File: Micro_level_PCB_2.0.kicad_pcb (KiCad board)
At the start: 2 copper layers, 203.2 x 44.5 mm, 105 parts, among them J5 Conn_01x06, J6 Conn_01x07_Female, Q1 SI2304DDS, Q2 SI2304DDS, Q3 SI2304DDS, Q4 SI2304DDS, Q5 SI2304DDS, SW1 FSM2JSMAA, SW2 FSM2JSMAA, SW3 FSM2JSMAA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

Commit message: 4 button up/down
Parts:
- added SW6: FSM2JSMAA, MY_KICAD_LIB:SW_Push_1P1T_NO_6x6mm_H5.0mm, F.Cu at (15.9, 38.1)
- added SW7: FSM2JSMAA, MY_KICAD_LIB:SW_Push_1P1T_NO_6x6mm_H5.0mm, F.Cu at (15.9, 6.35)
- D1: value SMF18A -> 1PGSMA4740HR3G
- moved J6 19.4 mm to (4.08, 23.6), turned to -90 degrees
- moved C16 17.9 mm to (25.8, 20.8)
- moved L1 15.0 mm to (28.1, 20.9), turned to 90 degrees
- moved SW4 6.35 mm to (31.8, 38.1), turned to 90 degrees
- moved SW5 6.35 mm to (31.8, 6.35), turned to 90 degrees
- renumbered Dimmer to Dim1, Power to Power1, Sensors to Sensors1, Solenoids to Solenoids1
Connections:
- net DOWN renamed Right_DOWN
- net UP renamed Right_UP
- J6 pad 7: OUTSIDE_VALID -> unconnected-(J6-Pad7)
- U1 pad 1: REMOTE_TRAVEL -> Left_UP
- U1 pad 11: POWERUP -> unconnected-(U1-Pad11)
- U1 pad 2: REMOTE_DOWN -> unconnected-(U1-Pad2)
- U1 pad 25: SPARE1 -> unconnected-(U1-Pad25)
- U1 pad 3: REMOTE_UP -> unconnected-(U1-Pad3)
- U1 pad 43: REMOTE_CAMP -> REMOTE_RU
- U1 pad 44: REMOTE_RU -> Left_DOWN
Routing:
- net Left_UP: track 0.00 -> 54.6 mm, vias 0 -> 2
- net Left_DOWN: track 0.00 -> 33.7 mm
- net Net-(C16-Pad2): track 6.57 -> 24.1 mm
- net REMOTE_LD: track 28.2 -> 41.4 mm, vias 1 -> 0
- net REMOTE_LU: track 26.0 -> 38.6 mm, vias 1 -> 0
- net REMOTE_RD: track 26.9 -> 35.7 mm, vias 1 -> 0
- net Right_DOWN: track 37.5 -> 30.4 mm
- net V5: track 233.7 -> 227.5 mm
- net RX: track 39.1 -> 42.9 mm
- net Right_UP: track 29.9 -> 32.5 mm, vias 2 -> 4
- net REMOTE_RU: track 28.9 -> 29.8 mm, vias 1 -> 0

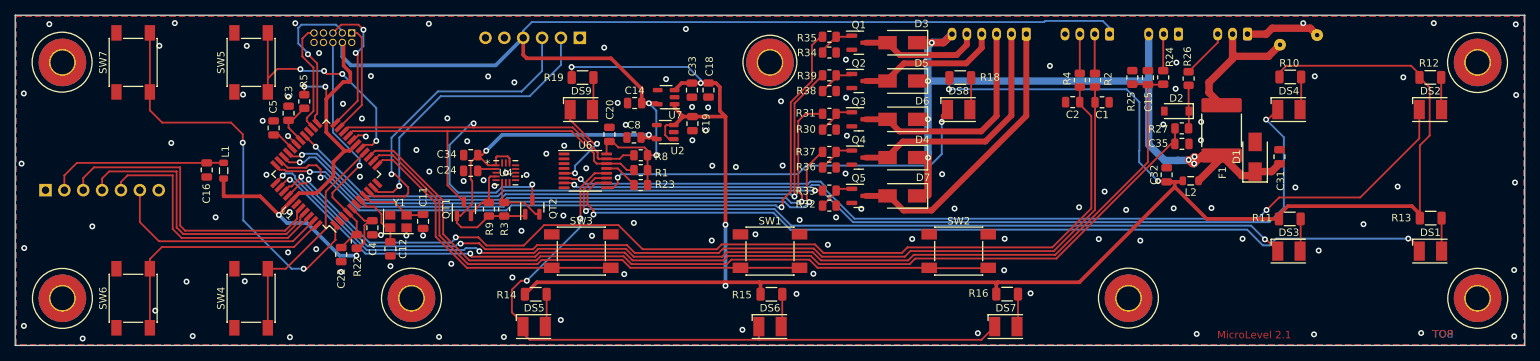
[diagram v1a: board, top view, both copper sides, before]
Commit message: move buttons, change jtag connector
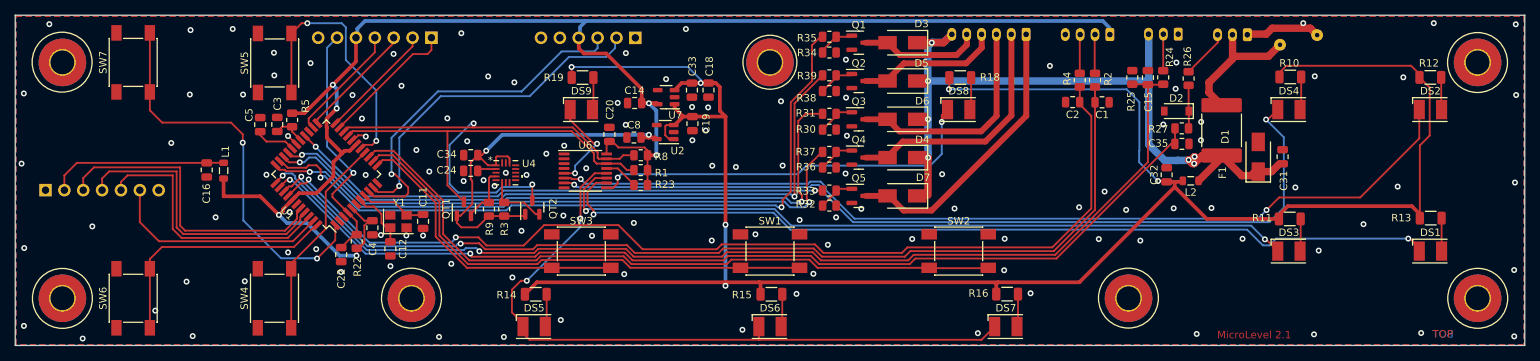
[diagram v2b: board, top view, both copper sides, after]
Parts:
- removed CX1: Conn2x5_CNC#3220-10-0100-00, Connector_PinSocket_1.27mm:PinSocket_2x05_P1.27mm_Vertical
- removed Dim1, Power1: B3B-PH-K-S, Connector_JST:JST_PH_B3B-PH-K_1x03_P2.00mm_Vertical
- removed Sensors1: B4B-PH-K-S, Connector_JST:JST_PH_B4B-PH-K_1x04_P2.00mm_Vertical
- removed Solenoids1: B6B-PH-K-S, Connector_JST:JST_PH_B6B-PH-K_1x06_P2.00mm_Vertical
- added J1: Conn_01x07_Female, Connector_PinHeader_2.54mm:PinHeader_1x07_P2.54mm_Vertical, B.Cu at (56.0, 3.02)
- added J2: B6B-PH-K-S, Connector_JST:JST_PH_B6B-PH-K_1x06_P2.00mm_Vertical, B.Cu at (136.1, 2.58)
- added J3: B3B-PH-K-S, Connector_JST:JST_PH_B3B-PH-K_1x03_P2.00mm_Vertical, B.Cu at (156.6, 2.55)
- added J4: B3B-PH-K-S, Connector_JST:JST_PH_B3B-PH-K_1x03_P2.00mm_Vertical, B.Cu at (165.8, 2.62)
- added j7: B4B-PH-K-S, Connector_JST:JST_PH_B4B-PH-K_1x04_P2.00mm_Vertical, B.Cu at (147.3, 2.60)
- moved J5 7.47 mm to (83.5, 3.04)
- moved SW5 3.18 mm to (34.9, 6.42)
- moved SW4 3.15 mm to (34.9, 38.1)
- moved R5 2.98 mm to (37.3, 14.1)
- moved C3 2.14 mm to (35.3, 14.7)
- moved C5 1.86 mm to (33.0, 14.7)
- moved D1 0.42 mm to (167.3, 19.1)
- moved C31 0.42 mm to (170.6, 19.1)
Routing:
- net V5: track 227.5 -> 216.4 mm
- net TDO: track 20.9 -> 15.1 mm, vias 1 -> 0
- net TX: track 40.1 -> 45.9 mm
- net RX: track 42.9 -> 48.6 mm
- net TMS: track 19.3 -> 15.9 mm, vias 2 -> 0
- net Right_DOWN: track 30.4 -> 26.9 mm
- net TCK: track 15.0 -> 18.4 mm
- net Right_UP: track 32.5 -> 35.9 mm, vias 4 -> 2
- net VLED: track 285.8 -> 283.2 mm
- net Net-(C5-Pad1): track 3.26 -> 5.52 mm
- net Net-(C3-Pad2): track 6.13 -> 4.53 mm
- net LED_ACTIVE: track 95.2 -> 93.9 mm
- net Left_UP: track 54.6 -> 53.4 mm
- net TDI: track 15.2 -> 16.0 mm
- net Net-(C12-Pad1): track 8.25 -> 7.54 mm
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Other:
- board text added: "Compress"
- board text added: "Sensors"
- board text added: "Solenoids"
- board text removed: "Compressor"

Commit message: move resistor
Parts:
- moved R5 0.55 mm to (37.3, 13.6)
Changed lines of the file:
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@@
   )
   (footprint "Resistor_SMD:R_0805_2012Metric" (layer "F.Cu")
-    (at 37.275 14.1 90)
+    (at 37.325 13.55 90)
     (descr "Resistor SMD 0805 (2012 Metric), square (rectangular) end terminal, IPC_7351 nominal, (Body size source: IPC-SM-782 page 72, https://www.pcb-3d.com/wordpress/wp-content/uploads/ipc-sm-782a_amendment_1_and_2.pdf), generated with kicad-footprint-generator")
     (tags "resistor")
@@
     (fp_line (start 11.95 -2.8) (end 11.95 1.7) (layer "B.Fab") (width 0.1))
     (fp_line (start -1.95 1.7) (end -1.95 -2.8) (layer "B.Fab") (width 0.1))
-    (pad "1" thru_hole roundrect (at 0 0 180) (size 1.2 1.75) (drill 0.75) (layers *.Cu *.Mask) (roundrect_rratio 0.208333)
+    (pad "1" thru_hole roundrect (at 0 0 180) (size 1.2 1.75) (drill 0.75) (layers *.Cu *.Mask) (roundrect_rratio 0.2083333333)
       (net 41 "COMPRELAY") (pinfunction "Pin_1") (pintype "passive"))
     (pad "2" thru_hole oval (at 2 0 180) (size 1.2 1.75) (drill 0.75) (layers *.Cu *.Mask)
@@
     (fp_line (start -1.95 1.7) (end -1.95 -2.8) (layer "B.Fab") (width 0.1))
     (fp_line (start -1.95 -2.8) (end 5.95 -2.8) (layer "B.Fab") (width 0.1))
-    (pad "1" thru_hole roundrect (at 0 0 180) (size 1.2 1.75) (drill 0.75) (layers *.Cu *.Mask) (roundrect_rratio 0.208333)
+    (pad "1" thru_hole roundrect (at 0 0 180) (size 1.2 1.75) (drill 0.75) (layers *.Cu *.Mask) (roundrect_rratio 0.2083333333)
       (net 85 "GND") (pinfunction "Pin_1") (pintype "passive"))
     (pad "2" thru_hole oval (at 2 0 180) (size 1.2 1.75) (drill 0.75) (layers *.Cu *.Mask)
@@
     (fp_line (start -1.95 -2.8) (end 7.95 -2.8) (layer "B.Fab") (width 0.1))
     (fp_line (start -2.36 2.11) (end -2.36 0.86) (layer "B.Fab") (width 0.1))
-    (pad "1" thru_hole roundrect (at 0 0 180) (size 1.2 1.75) (drill 0.75) (layers *.Cu *.Mask) (roundrect_rratio 0.208333)
+    (pad "1" thru_hole roundrect (at 0 0 180) (size 1.2 1.75) (drill 0.75) (layers *.Cu *.Mask) (roundrect_rratio 0.2083333333)
       (net 84 "V5") (pinfunction "Pin_1") (pintype "passive"))
     (pad "2" thru_hole oval (at 2 0 180) (size 1.2 1.75) (drill 0.75) (layers *.Cu *.Mask)
@@
     (fp_line (start -1.95 1.7) (end -1.95 -2.8) (layer "B.Fab") (width 0.1))
     (fp_line (start 5.95 -2.8) (end 5.95 1.7) (layer "B.Fab") (width 0.1))
-    (pad "1" thru_hole roundrect (at 0 0 180) (size 1.2 1.75) (drill 0.75) (layers *.Cu *.Mask) (roundrect_rratio 0.208333)
+    (pad "1" thru_hole roundrect (at 0 0 180) (size 1.2 1.75) (drill 0.75) (layers *.Cu *.Mask) (roundrect_rratio 0.2083333333)
       (net 85 "GND") (pinfunction "Pin_1") (pintype "passive"))
     (pad "2" thru_hole oval (at 2 0 180) (size 1.2 1.75) (drill 0.75) (layers *.Cu *.Mask)
@@
   (segment (start 85.3 16.1) (end 65.55 16.1) (width 0.5) (layer "B.Cu") (net 1))
   (segment (start 65.55 16.1) (end 63.4 18.25) (width 0.5) (layer "B.Cu") (net 1))
+  (segment (start 37.325 14.4625) (end 36.1375 15.65) (width 0.25) (layer "F.Cu") (net 2))
   (segment (start 38.415177 16.803806) (end 37.275 15.663629) (width 0.254) (layer "F.Cu") (net 2))
-  (segment (start 35.9125 15.0125) (end 35.275 15.65) (width 0.254) (layer "F.Cu") (net 2))
-  (segment (start 37.275 15.0125) (end 35.9125 15.0125) (width 0.254) (layer "F.Cu") (net 2))
+  (segment (start 36.1375 15.65) (end 35.275 15.65) (width 0.25) (layer "F.Cu") (net 2))
   (segment (start 37.275 15.663629) (end 37.275 15.0125) (width 0.254) (layer "F.Cu") (net 2))
   (segment (start 95.61 13.64) (end 94.85 12.88) (width 0.5) (layer "F.Cu") (net 3))
@@
   (segment (start 37.2 22.15) (end 36.97 22.15) (width 0.254) (layer "B.Cu") (net 82))
   (segment (start 43.9 18.45) (end 44.02 18.57) (width 0.25) (layer "F.Cu") (net 84))
-  (segment (start 38.9375 13.1875) (end 37.275 13.1875) (width 0.5) (layer "F.Cu") (net 84))
   (segment (start 37.283806 24.864823) (end 36.05 26.098629) (width 0.5) (layer "F.Cu") (net 84))
   (segment (start 45.865 6.09) (end 45.865 3.025) (width 0.5) (layer "F.Cu") (net 84))
@@
   (segment (start 41.907298 15.063336) (end 41.95 15.106038) (width 0.5) (layer "F.Cu") (net 84))
   (segment (start 45.97 31.3625) (end 45.97 32.33) (width 0.254) (layer "F.Cu") (net 84))
-  (segment (start 42.75 9.375) (end 38.9375 13.1875) (width 0.5) (layer "F.Cu") (net 84))
   (segment (start 46.2875 31.3625) (end 47 30.65) (width 0.254) (layer "F.Cu") (net 84))
   (segment (start 86.3225 11.82) (end 86.4825 11.98) (width 0.5) (layer "F.Cu") (net 84))
@@
   (segment (start 42.83 19.76) (end 42.83 21.69) (width 0.5) (layer "F.Cu") (net 84))
   (segment (start 79.6025 18.675) (end 79.6025 17.3675) (width 0.254) (layer "F.Cu") (net 84))
+  (segment (start 37.3375 12.625) (end 37.325 12.6375) (width 0.5) (layer "F.Cu") (net 84))
   (segment (start 41.95 16.5) (end 43.9 18.45) (width 0.5) (layer "F.Cu") (net 84))
   (segment (start 45.97 32.33) (end 45.94 32.36) (width 0.254) (layer "F.Cu") (net 84))
@@
   (segment (start 45.875 6.25) (end 45.875 6.1) (width 0.25) (layer "F.Cu") (net 84))
   (segment (start 36.05 26.331734) (end 35.49457 26.887164) (width 0.5) (layer "F.Cu") (net 84))
+  (segment (start 42.75 9.375) (end 39.5 12.625) (width 0.5) (layer "F.Cu") (net 84))
   (segment (start 47 28.3) (end 47.64 27.66) (width 0.254) (layer "F.Cu") (net 84))
   (segment (start 76.55 5.15) (end 75.855 4.455) (width 0.5) (layer "F.Cu") (net 84))
+  (segment (start 39.5 12.625) (end 37.3375 12.625) (width 0.5) (layer "F.Cu") (net 84))
   (segment (start 80.39 16.99) (end 81.2 17.8) (width 0.254) (layer "F.Cu") (net 84))
   (via (at 42.75 9.375) (size 0.8) (drill 0.4) (layers "F.Cu" "B.Cu") (net 84))

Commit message: fix compressor text
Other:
- board text added: "Compressor"
- board text removed: "Compress"
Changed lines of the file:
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@@
     (effects (font (size 2 2) (thickness 0.3)) (justify mirror))
   )
-  (gr_text "Compress" (at 136.225 10.425 90) (layer "B.SilkS")
+  (gr_text "Compressor" (at 136.125 10.325 90) (layer "B.SilkS")
     (effects (font (size 1 1) (thickness 0.15)) (justify mirror))
   )
